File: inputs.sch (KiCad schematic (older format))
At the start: 36 parts

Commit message: Agrego v1.0 de SmartSaffron
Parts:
- C201: renamed from C?; footprint (none) -> 00_lib_fp:C_0805_2012Metric_Pad1.18x1.45mm_HandSolder; symbol Device:CP1 -> 00_lib_sch:CP1
- C202: renamed from C?; footprint (none) -> 00_lib_fp:C_0805_2012Metric_Pad1.18x1.45mm_HandSolder; symbol Device:C -> 00_lib_sch:C
- R201, R202, R203, R204, R205, R206, R207, R208, R209, R210, R211, R212, R213, R214, R215, R216, R217, R218, R219, R220, R221, R222, R223, R224, R225: renamed from R?; footprint (none) -> 00_lib_fp:R_0805_2012Metric_Pad1.20x1.40mm_HandSolder; symbol Device:R -> 00_lib_sch:R
- U201: renamed from U?; footprint Package_SO:TSSOP-24_4.4x7.8mm_P0.65mm -> 00_lib_fp:TSSOP-24_4.4x7.8mm_P0.65mm; symbol 00_lib_sch:Interface_Expansion_TCA9548APWR -> 00_lib_sch:TCA9548APWR
- gave numbers to parts that had none: 8
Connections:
- net labels added: SC0, SC1, SC2, SC3, SC4, SC5, SC6, SC7, SD0, SD1, SD2, SD3, SD4, SD5, SD6, SD7
- wire segments 128 -> 112
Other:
- note added: "INPUTS"
- moved on the sheet: C201

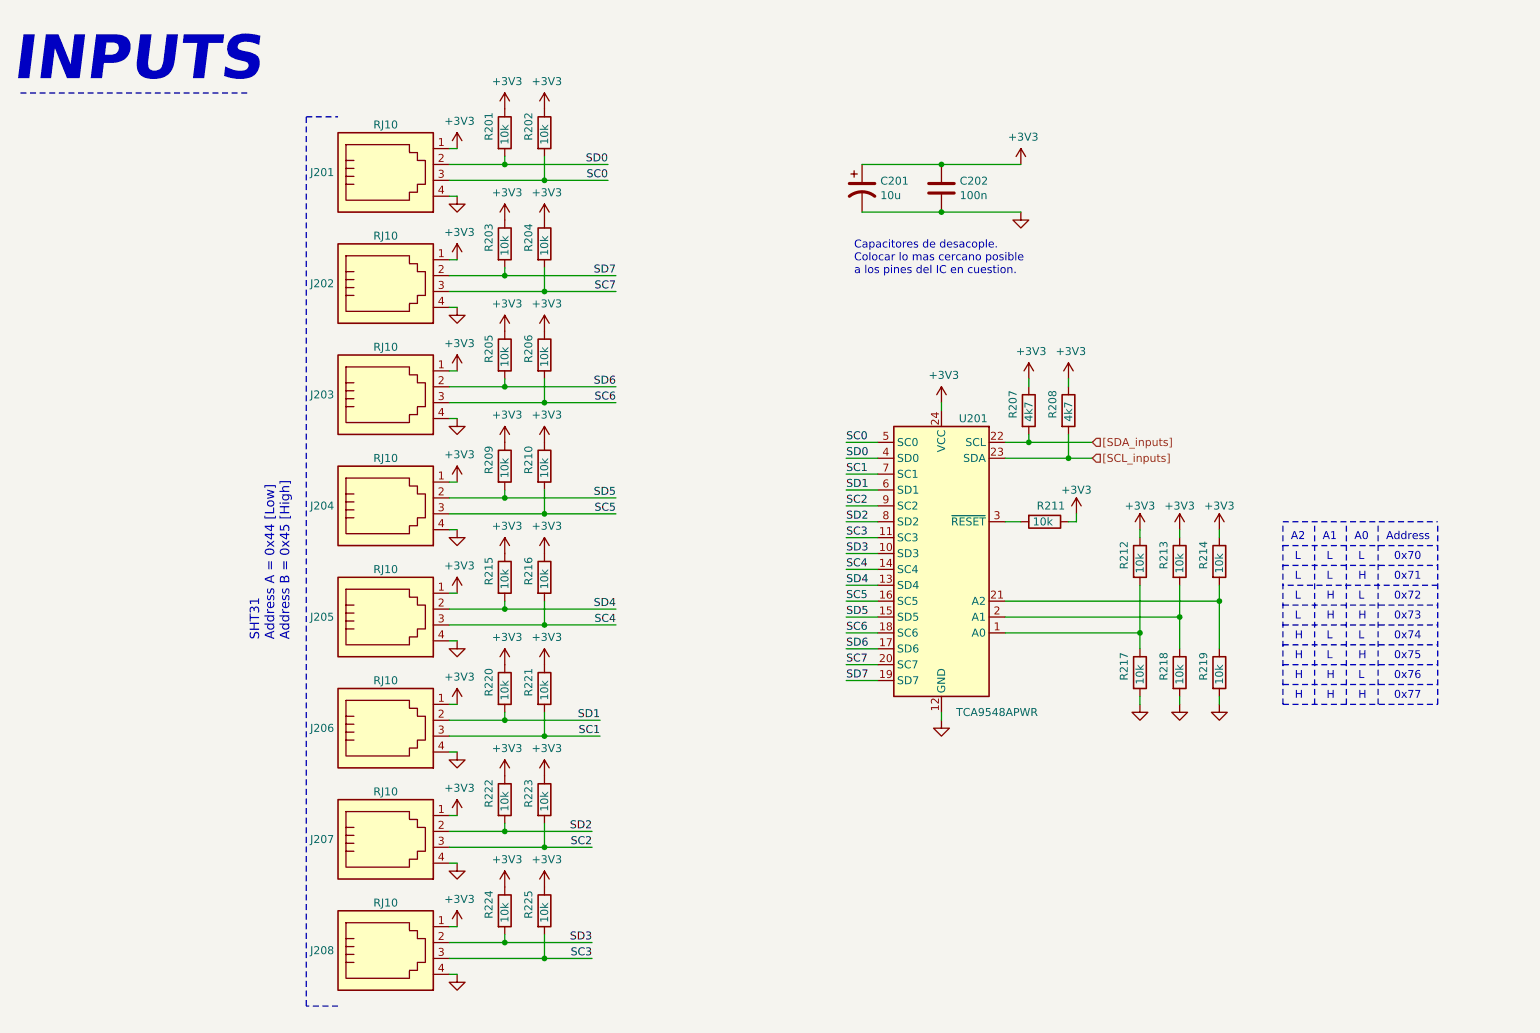
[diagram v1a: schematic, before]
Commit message: Fix por revision grupal
    *Fix de memoria de i2c, mal sda y scl
    *Fix inpunts sda y scl
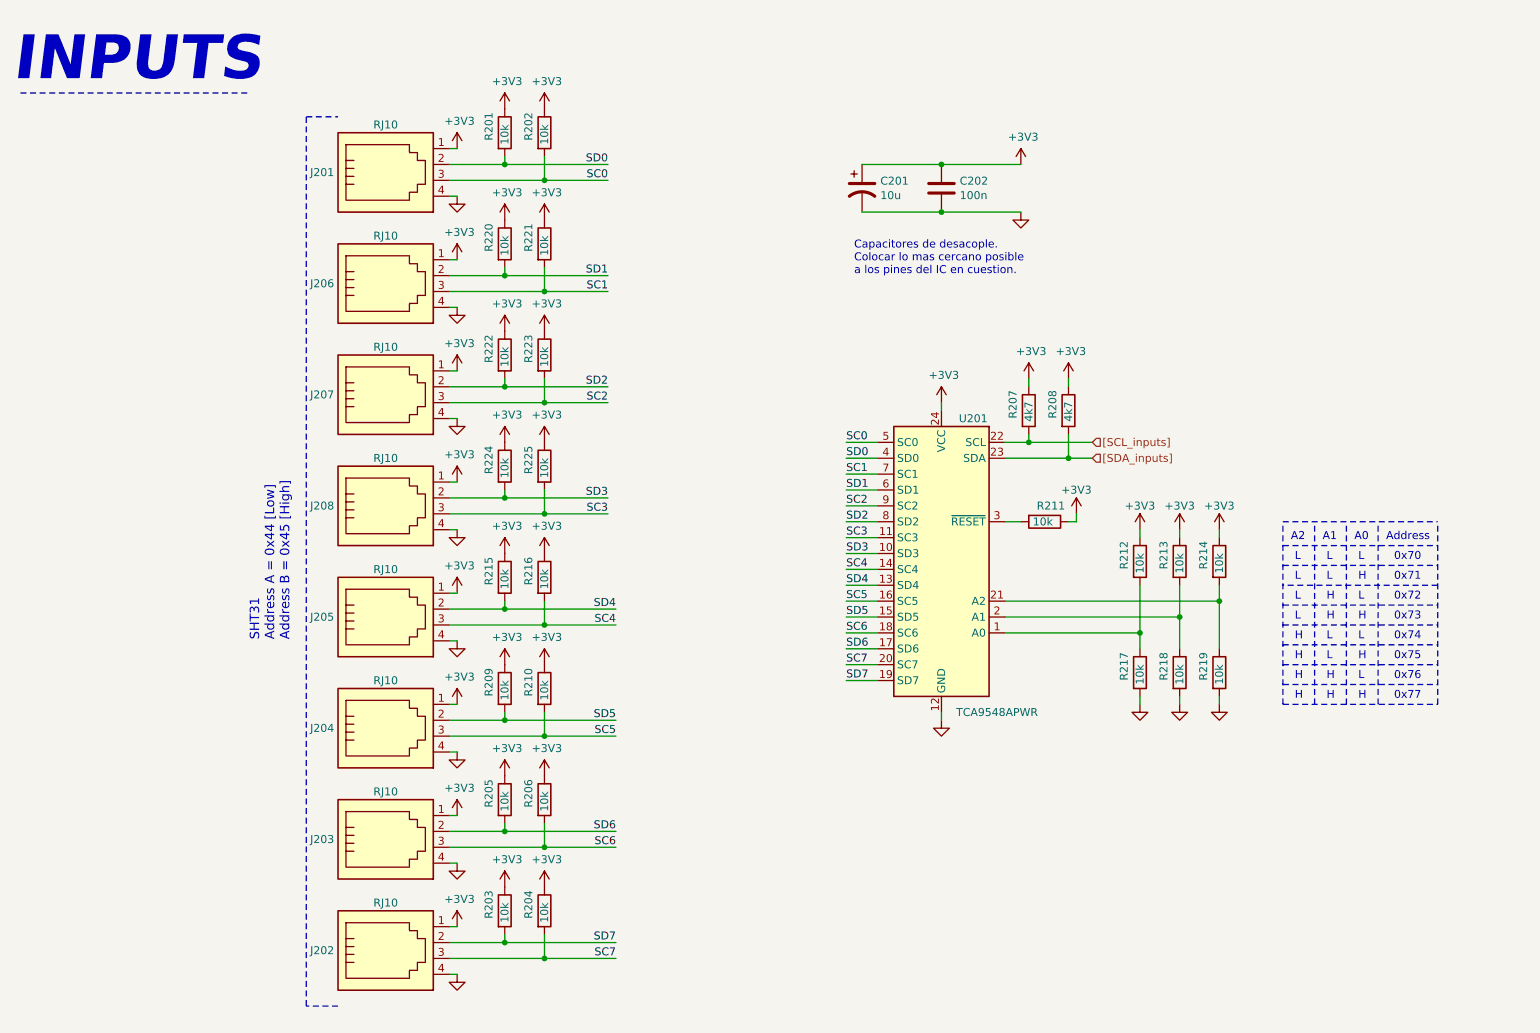
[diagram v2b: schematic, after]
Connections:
- net [SCL_inputs]: now also R207.2, U201.22 (SCL); no longer R208.2, U201.23 (SDA)
- net [SDA_inputs]: now also R208.2, U201.23 (SDA); no longer R207.2, U201.22 (SCL)
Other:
- moved on the sheet: J202, J203, J204, J206, J207, J208, R203, R204, R205, R206, R209, R210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
